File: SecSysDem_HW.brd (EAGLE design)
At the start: 99 x 78 mm, 58 parts, among them IC1 L7805 5V, Q1 2N3904, T1 MOSFET_NCHANNEL_ENHANCEMENT2N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, T2 MOSFET_NCHANNEL_ENHANCEMENT2N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, T3 MOSFET_NCHANNEL_ENHANCEMENT2N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, U1 XPLAINED_MINI_PINOUT, U2 PCF8574_IO_EXPANDER, U4 FT24C512A, U5 MCP4901-E/SN, X1 C-GRID-06-70553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

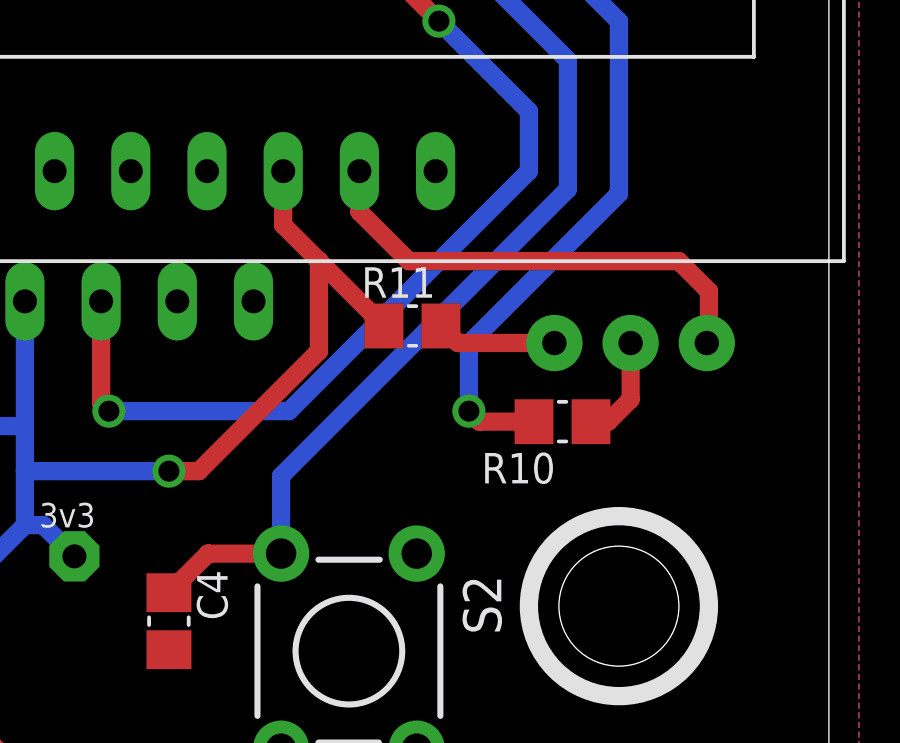
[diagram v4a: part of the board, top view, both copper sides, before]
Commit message: Changed the pins so that the backlight is on PD6 instead of PD7 for pwm.
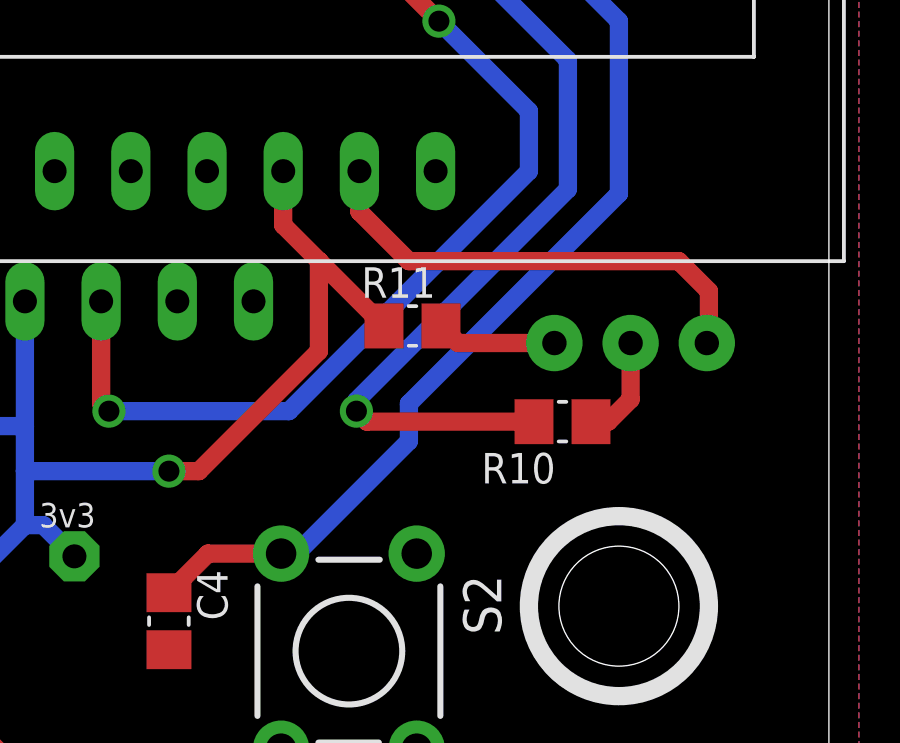
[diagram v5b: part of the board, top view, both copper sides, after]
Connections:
- net LCD_BACKLIGHT: now also U1.P$21; no longer U1.P$22
- net PUSH_BUTTON: now also U1.P$22; no longer U1.P$21
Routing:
- net LCD_BACKLIGHT: track 74.5 -> 78.0 mm
- net PUSH_BUTTON: track 82.0 -> 84.1 mm
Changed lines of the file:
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@@
 </signal>
 <signal name="LCD_BACKLIGHT">
-<contactref element="R10" pad="1"/>
-<contactref element="U1" pad="P$22"/>
-<wire x1="62.04" y1="63.92" x2="62" y2="63.88" width="0.6096" layer="16"/>
-<wire x1="62" y1="63.88" x2="62" y2="61" width="0.6096" layer="16"/>
-<wire x1="62" y1="61" x2="60" y2="59" width="0.6096" layer="16"/>
-<wire x1="60" y1="59" x2="60" y2="50" width="0.6096" layer="16"/>
-<wire x1="60" y1="50" x2="81" y2="29" width="0.6096" layer="16"/>
-<wire x1="81" y1="29" x2="88" y2="29" width="0.6096" layer="16"/>
-<wire x1="88" y1="29" x2="92" y2="25" width="0.6096" layer="16"/>
-<wire x1="92" y1="25" x2="92" y2="19.25" width="0.6096" layer="16"/>
-<wire x1="92" y1="19.25" x2="87" y2="14.25" width="0.6096" layer="16"/>
-<wire x1="87" y1="14.25" x2="87" y2="12" width="0.6096" layer="16"/>
-<via x="87" y="12" extent="1-16" drill="0.7"/>
-<wire x1="87" y1="12" x2="87.35" y2="11.65" width="0.6096" layer="1"/>
-<wire x1="87.35" y1="11.65" x2="89.17" y2="11.65" width="0.6096" layer="1"/>
-</signal>
-<signal name="PUSH_BUTTON">
-<contactref element="S2" pad="3" route="any" routetag="G$1.2"/>
-<contactref element="S2" pad="4" route="any" routetag="G$1.2"/>
-<contactref element="C4" pad="1"/>
-<wire x1="77" y1="5.95" x2="78.3012" y2="7.2512" width="0.6096" layer="1"/>
-<wire x1="78.3012" y1="7.2512" x2="80.7394" y2="7.2512" width="0.6096" layer="1"/>
 <contactref element="U1" pad="P$21"/>
 <wire x1="59.5" y1="63.92" x2="59.5" y2="60.75" width="0.6096" layer="16"/>
@@
 <wire x1="87" y1="27" x2="90.3" y2="23.7" width="0.6096" layer="16"/>
 <wire x1="90.3" y1="23.7" x2="90.3" y2="19.4" width="0.6096" layer="16"/>
-<wire x1="90.3" y1="19.4" x2="80.7394" y2="9.8394" width="0.6096" layer="16"/>
-<wire x1="80.7394" y1="9.8394" x2="80.7394" y2="7.2512" width="0.6096" layer="16"/>
+<wire x1="90.3" y1="19.4" x2="83.25" y2="12.35" width="0.6096" layer="16"/>
+<contactref element="R10" pad="1"/>
+<wire x1="83.25" y1="12.35" x2="83.25" y2="12" width="0.6096" layer="16"/>
+<via x="83.25" y="12" extent="1-16" drill="0.7"/>
+<wire x1="83.25" y1="12" x2="83.6" y2="11.65" width="0.6096" layer="1"/>
+<wire x1="83.6" y1="11.65" x2="89.17" y2="11.65" width="0.6096" layer="1"/>
 </signal>
 <signal name="KEYPAD_1">
@@
 </polygon>
 </signal>
+<signal name="PUSH_BUTTON">
+<contactref element="S2" pad="3" route="any" routetag="G$1.2"/>
+<contactref element="S2" pad="4" route="any" routetag="G$1.2"/>
+<contactref element="C4" pad="1"/>
+<wire x1="77" y1="5.95" x2="78.3012" y2="7.2512" width="0.6096" layer="1"/>
+<wire x1="78.3012" y1="7.2512" x2="80.7394" y2="7.2512" width="0.6096" layer="1"/>
+<contactref element="U1" pad="P$22"/>
+<wire x1="62.04" y1="63.92" x2="62" y2="63.88" width="0.6096" layer="16"/>
+<wire x1="62" y1="63.88" x2="62" y2="61" width="0.6096" layer="16"/>
+<wire x1="62" y1="61" x2="60" y2="59" width="0.6096" layer="16"/>
+<wire x1="60" y1="59" x2="60" y2="50" width="0.6096" layer="16"/>
+<wire x1="60" y1="50" x2="81" y2="29" width="0.6096" layer="16"/>
+<wire x1="81" y1="29" x2="88" y2="29" width="0.6096" layer="16"/>
+<wire x1="88" y1="29" x2="92" y2="25" width="0.6096" layer="16"/>
+<wire x1="92" y1="25" x2="92" y2="19.25" width="0.6096" layer="16"/>
+<wire x1="92" y1="19.25" x2="85" y2="12.25" width="0.6096" layer="16"/>
+<wire x1="85" y1="12.25" x2="85" y2="11" width="0.6096" layer="16"/>
+<wire x1="85" y1="11" x2="81.2512" y2="7.2512" width="0.6096" layer="16"/>
+<wire x1="81.2512" y1="7.2512" x2="80.7394" y2="7.2512" width="0.6096" layer="16"/>
+</signal>
 </signals>

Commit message: Made board mods to schematic
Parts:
- added C5: 1uF, Luke:C0805
- R11: value 100 -> 10k
- moved R11 117.2 mm to (-28.0, -16.0)
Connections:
- net +3V3: no longer R11.1, R7.2
- net +5V: now also R11.2, R7.2
- net GND: now also Q1.3
- net N$18: now also U$3.P$15, U$3.P$7; no longer R11.2
- net N$19: now also C5.2, U5.8; no longer Q1.3, U$3.P$15, U$3.P$7
- net N$3: now also C5.1, R11.1; no longer U5.8
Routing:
- net N$19: track 15.9 -> 0.00 mm
- net +3V3: track 258.1 -> 250.3 mm
- net N$18: track 4.02 -> 0.00 mm
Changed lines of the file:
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@@
 <attribute name="NAME" x="87.4182" y="9.5898" size="1.016" layer="25" font="vector" ratio="15"/>
 </element>
-<element name="R11" library="Luke" package="C0805" value="100" x="85.12" y="14.84"/>
 <element name="D1" library="diode" package="DO41-7.6" value="1N5819-T" x="7.66" y="29.24" smashed="yes" rot="MR180">
 <attribute name="NAME" x="7.372" y="30.411" size="1.27" layer="26" ratio="10" rot="MR0"/>
@@
 <element name="U$1" library="Luke" package="NINJA_TURTLE1" value="" x="42" y="35"/>
 <element name="U$4" library="Luke" package="NINJA_TURTLE2" value="" x="30" y="35" rot="SR0"/>
+<element name="R11" library="Luke" package="C0805" value="10k" x="-28" y="-16"/>
+<element name="C5" library="Luke" package="C0805" value="1uF" x="-28" y="-20"/>
 </elements>
 <signals>
@@
 <wire x1="51.565" y1="-3.1" x2="51.565" y2="-6.435" width="0.6096" layer="1"/>
 <wire x1="51.565" y1="-6.435" x2="51" y2="-7" width="0.6096" layer="1"/>
+<contactref element="Q1" pad="3"/>
+<wire x1="85.89" y1="20" x2="94.93" y2="14.27" width="0" layer="19" extent="1-1"/>
 </signal>
 <signal name="I2C_SDA">
@@
 <wire x1="12" y1="25" x2="16" y2="29" width="0.6096" layer="16"/>
 <wire x1="16" y1="29" x2="23.5" y2="29" width="0.6096" layer="16"/>
+<contactref element="R7" pad="2"/>
+<contactref element="R11" pad="2"/>
+<wire x1="28" y1="59" x2="40.07" y2="48.74" width="0" layer="19" extent="1-1"/>
+<wire x1="-27.05" y1="-16" x2="5.09" y2="20" width="0" layer="19" extent="1-1"/>
 </signal>
 <signal name="+3V3">
@@
 <contactref element="V8" pad="P$1"/>
 <contactref element="V9" pad="P$1"/>
-<contactref element="R7" pad="2"/>
-<contactref element="R11" pad="1"/>
 <contactref element="U2" pad="2"/>
 <contactref element="U2" pad="1"/>
@@
 <contactref element="JP6" pad="3"/>
 <contactref element="U5" pad="1"/>
-<wire x1="84.17" y1="14.84" x2="82.005" y2="17.005" width="0.6096" layer="1"/>
 <wire x1="82.005" y1="17.005" x2="80.81" y2="18.2" width="0.6096" layer="1"/>
 <wire x1="80.81" y1="18.2" x2="80.81" y2="20" width="0.6096" layer="1"/>
@@
 <wire x1="39" y1="32" x2="31" y2="32" width="0.6096" layer="16"/>
 <via x="31" y="32" extent="1-16" drill="0.7"/>
-<wire x1="40.07" y1="48.74" x2="44.74" y2="48.74" width="0.6096" layer="1"/>
 <contactref element="R12" pad="2"/>
 <contactref element="R13" pad="2"/>
@@
 <signal name="N$3">
 <contactref element="T2" pad="1"/>
-<contactref element="U5" pad="8"/>
 <wire x1="38.91" y1="52.44" x2="41.44" y2="52.44" width="0.6096" layer="1"/>
 <wire x1="41.44" y1="52.44" x2="42" y2="53" width="0.6096" layer="1"/>
 <wire x1="42" y1="53" x2="42.305" y2="53" width="0.6096" layer="1"/>
-<wire x1="42.305" y1="53" x2="42.4" y2="53.095" width="0.6096" layer="1"/>
+<contactref element="R11" pad="1"/>
+<contactref element="C5" pad="1"/>
+<wire x1="-28.95" y1="-16" x2="38.91" y2="52.44" width="0" layer="19" extent="1-1"/>
+<wire x1="-28.95" y1="-20" x2="-28.95" y2="-16" width="0" layer="19" extent="1-1"/>
 </signal>
 <signal name="N$8">
@@
 <wire x1="91.65" y1="11.65" x2="92.39" y2="12.39" width="0.6096" layer="1"/>
 <wire x1="92.39" y1="12.39" x2="92.39" y2="14.27" width="0.6096" layer="1"/>
-</signal>
-<signal name="N$18">
-<contactref element="Q1" pad="1"/>
-<contactref element="R11" pad="2"/>
-<wire x1="86.07" y1="14.84" x2="86.64" y2="14.27" width="0.6096" layer="1"/>
-<wire x1="86.64" y1="14.27" x2="89.85" y2="14.27" width="0.6096" layer="1"/>
-</signal>
-<signal name="N$19">
-<contactref element="U$3" pad="P$15" route="any" routetag="G$1.LIGHT"/>
-<contactref element="U$3" pad="P$7" route="any" routetag="G$1.LIGHT"/>
-<contactref element="Q1" pad="3"/>
-<wire x1="94.93" y1="14.27" x2="95" y2="14.34" width="0.6096" layer="1"/>
-<wire x1="95" y1="14.34" x2="95" y2="16" width="0.6096" layer="1"/>
-<wire x1="95" y1="16" x2="94" y2="17" width="0.6096" layer="1"/>
-<wire x1="94" y1="17" x2="85" y2="17" width="0.6096" layer="1"/>
-<wire x1="85" y1="17" x2="83.35" y2="18.65" width="0.6096" layer="1"/>
-<wire x1="83.35" y1="18.65" x2="83.35" y2="20" width="0.6096" layer="1"/>
 </signal>
 <signal name="!DAC_CS">
@@
 <wire x1="81.2512" y1="7.2512" x2="80.7394" y2="7.2512" width="0.6096" layer="16"/>
 </signal>
+<signal name="N$18">
+<contactref element="U$3" pad="P$7" route="any" routetag="G$1.LIGHT"/>
+<contactref element="U$3" pad="P$15" route="any" routetag="G$1.LIGHT"/>
+<contactref element="Q1" pad="1"/>
+<wire x1="83.35" y1="20" x2="89.85" y2="14.27" width="0" layer="19" extent="1-1"/>
+</signal>
+<signal name="N$19">
+<contactref element="U5" pad="8"/>
+<contactref element="C5" pad="2"/>
+<wire x1="-27.05" y1="-20" x2="42.4" y2="53.095" width="0" layer="19" extent="1-1"/>
+</signal>
 </signals>
